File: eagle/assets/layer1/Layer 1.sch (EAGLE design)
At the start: 247 parts, among them M1C1 33nF, M1C2 680uF, M1C3 1.0uF, M1D1 RED, M1D2 BLUE, M1J1 XT30PB-F, M1Q1 AOD482, M1R1 1k, M1R10 1k, M1R11 10k, M1R12 4.7k, M1R2 1k, M1R3 3.3k, M1R4 3.3k, M1R5 1k, M1R6 1k, M1R7 1k, M1R8 10k, M1R9 10k, M2C1 33nF, M2C2 680uF, M2C3 1.0uF, M2D1 RED, M2D2 BLUE, M2J1 XT30PB-F, M2Q1 AOD482, M2R1 1k, M2R10 1k, M2R11 10k, M2R12 4.7k, M2R2 1k, M2R3 3.3k, M2R4 3.3k, M2R5 1k, M2R6 1k, M2R7 1k, M2R8 10k, M2R9 10k, M3C1 33nF, M3C2 680uF, M3C3 1.0uF, M3D1 RED, M3D2 BLUE, M3J1 XT30PB-F, M3Q1 AOD482, M3R1 1k, M3R10 1k, M3R11 10k, M3R12 4.7k, M3R2 1k, M3R3 3.3k, M3R4 3.3k, M3R5 1k, M3R6 1k, M3R7 1k, M3R8 10k, M3R9 10k, M4C1 33nF, M4C2 680uF, M4C3 1.0uF, M4D1 RED, M4D2 BLUE, M4J1 XT30PB-F, M4Q1 AOD482, M4R1 1k, M4R10 1k, M4R11 10k, M4R12 4.7k, M4R2 1k, M4R3 3.3k, M4R4 3.3k, M4R5 1k, M4R6 1k, M4R7 1k, M4R8 10k, M4R9 10k, Q1 LIGHT_SENSORALS, Q10 LIGHT_SENSORALS, Q11 LIGHT_SENSORALS, Q12 LIGHT_SENSORALS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

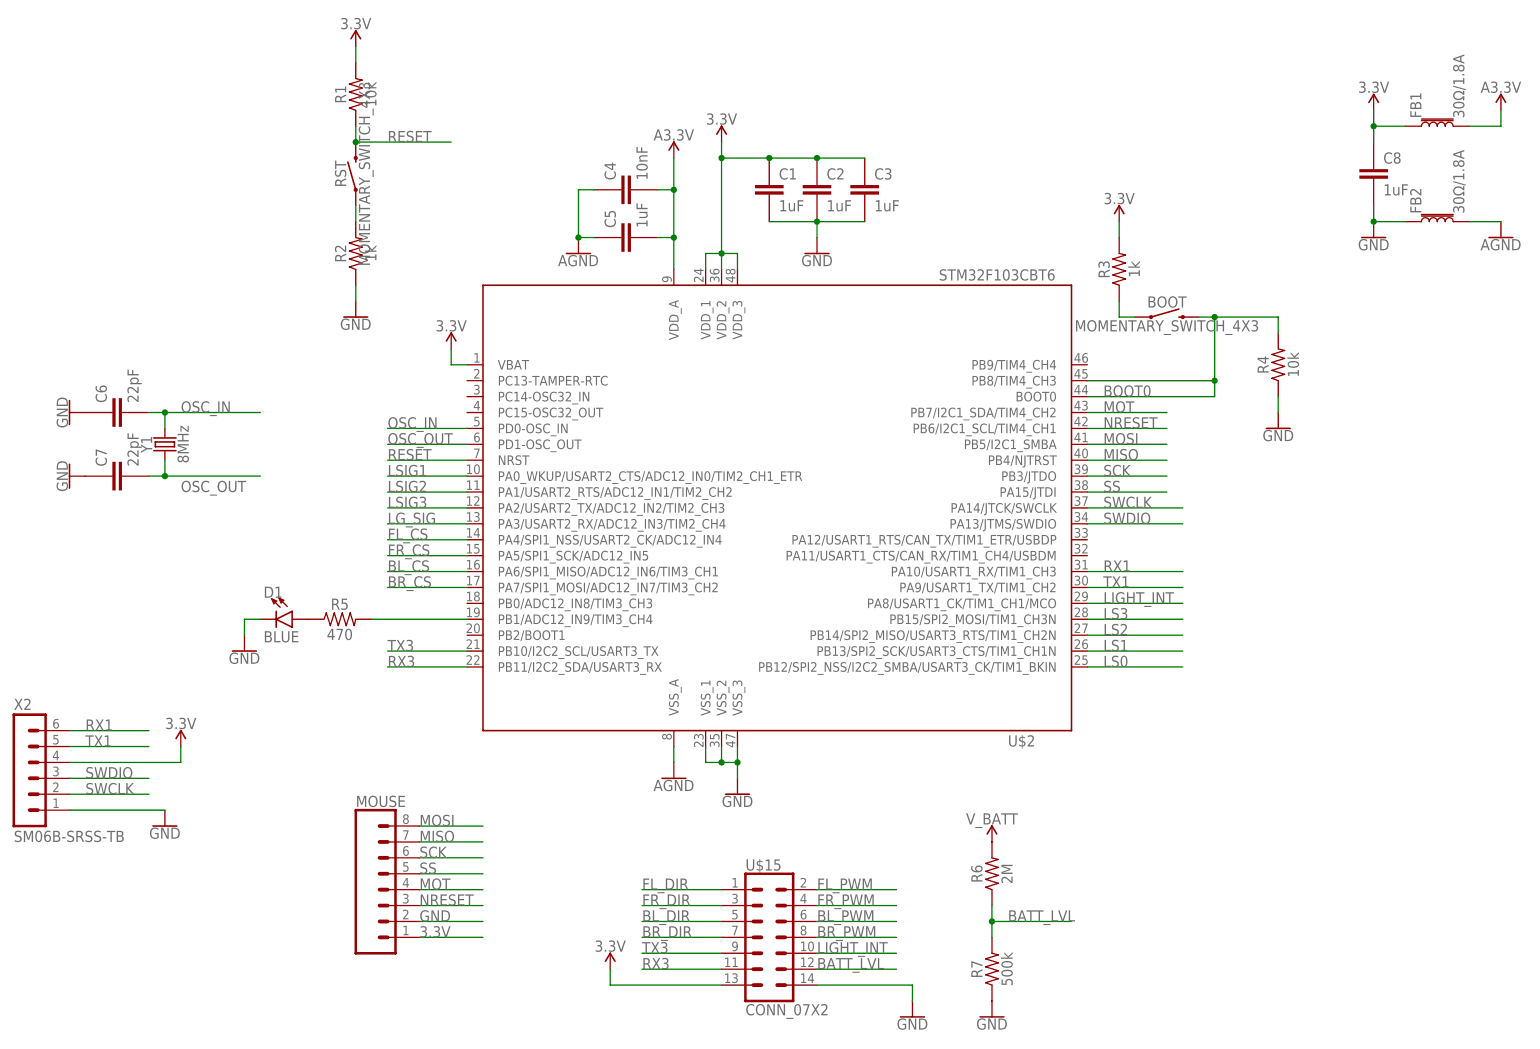
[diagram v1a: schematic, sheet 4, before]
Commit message: removed mouse sensor
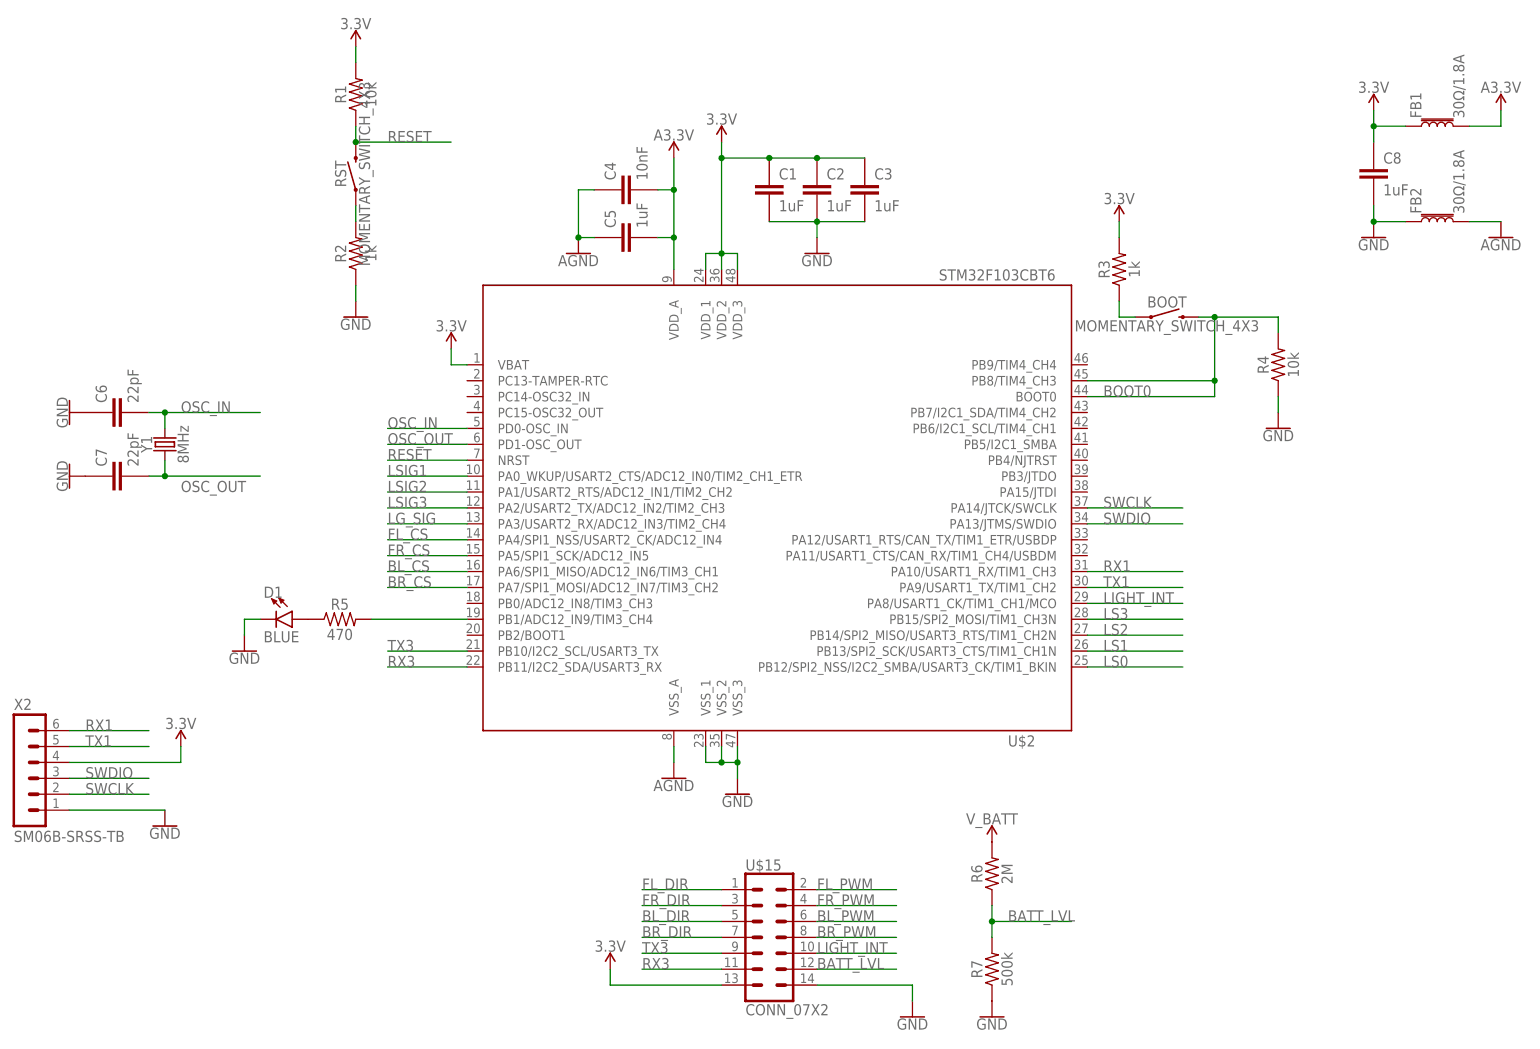
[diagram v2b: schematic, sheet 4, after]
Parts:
- removed LDR: (no value), SparkFun-Connectors:CONN_021X02_NO_SILK
- removed LED: (no value), SparkFun-Connectors:CONN_02POLAR
- removed LG_R2: 2k, JH:RESISTOR0603
- removed MOUSE: (no value), SparkFun-Connectors:CONN_08LOCK
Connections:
- removed net MISO: MOUSE.7, U$2.PB4/NJTRST
- removed net MOSI: MOUSE.8, U$2.PB5/I2C1_SMBA
- removed net MOT: MOUSE.4, U$2.PB7/I2C1_SDA/TIM4_CH2
- removed net NRESET: MOUSE.3, U$2.PB6/I2C1_SCL/TIM4_CH1
- removed net SCK: MOUSE.6, U$2.PB3/JTDO
- removed net SS: MOUSE.5, U$2.PA15/JTDI
- net 3.3V: no longer MOUSE.1
- net GND: no longer LED.1, LG_R2.1, MOUSE.2
- net LG_SIG: no longer LDR.2, LG_R2.2
- net LSWITCH: no longer LED.2
- net VCCA: no longer LDR.1

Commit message: depression
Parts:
- added LDR: (no value), SparkFun-Connectors:CONN_021X02_NO_SILK
- added LED: (no value), SparkFun-Connectors:CONN_02POLAR
- added LG_R2: 2k, JH:RESISTOR0603
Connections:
- net BL_OUTA: now also M3J1.V+; no longer M3J1.P$V+
- net BL_OUTB: now also M3J1.V-; no longer M3J1.P$V-
- net BR_OUTA: now also M4J1.V+; no longer M4J1.P$V+
- net BR_OUTB: now also M4J1.V-; no longer M4J1.P$V-
- net FL_OUTA: now also M1J1.V+; no longer M1J1.P$V+
- net FL_OUTB: now also M1J1.V-; no longer M1J1.P$V-
- net FR_OUTA: now also M2J1.V+; no longer M2J1.P$V+
- net FR_OUTB: now also M2J1.V-; no longer M2J1.P$V-
- net GND: now also ESC_OUT.V-, LED.1, LG_R2.1, U$1.V-; no longer ESC_OUT.P$V-, U$1.P$V-
- net LG_SIG: now also LDR.2, LG_R2.2
- net LSWITCH: now also LED.2
- net VCCA: now also LDR.1
- net V_BATT: now also ESC_OUT.V+, U$1.V+; no longer ESC_OUT.P$V+, U$1.P$V+

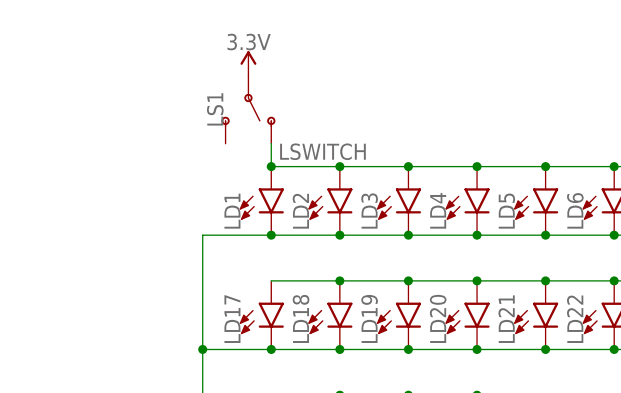
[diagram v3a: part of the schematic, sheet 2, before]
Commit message: edited layer 1
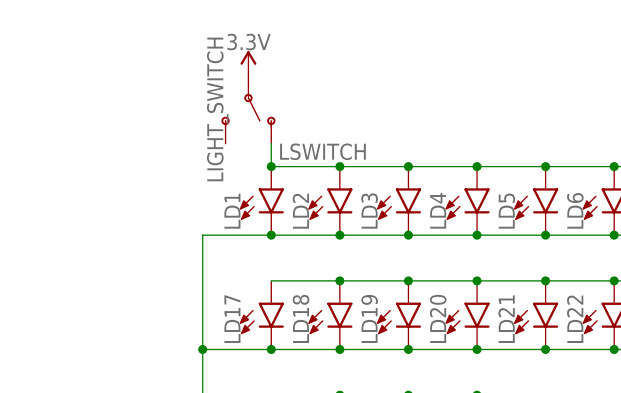
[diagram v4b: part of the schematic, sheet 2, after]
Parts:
- renumbered LS1 to LIGHT_SWITCH, S3 to MOTOR_SWITCH
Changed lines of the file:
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@@
 <part name="LD35" library="JH" library_urn="urn:adsk.eagle:library:6027132" deviceset="3528LED" device="" package3d_urn="urn:adsk.eagle:package:6740529/3"/>
 <part name="LD36" library="JH" library_urn="urn:adsk.eagle:library:6027132" deviceset="3528LED" device="" package3d_urn="urn:adsk.eagle:package:6740529/3"/>
-<part name="LS1" library="SparkFun-Switches" library_urn="urn:adsk.eagle:library:11044690" deviceset="SWITCH-SPDT" device="-PTH-11.6X4.0MM-LOCK" package3d_urn="urn:adsk.eagle:package:11044812/2"/>
+<part name="LIGHT_SWITCH" library="SparkFun-Switches" library_urn="urn:adsk.eagle:library:11044690" deviceset="SWITCH-SPDT" device="-PTH-11.6X4.0MM-LOCK" package3d_urn="urn:adsk.eagle:package:11044812/2"/>
 <part name="GND19" library="SparkFun-PowerSymbols" deviceset="GND" device=""/>
 <part name="LC1" library="JH" library_urn="urn:adsk.eagle:library:6027132" deviceset="CAPACITOR" device="0603" package3d_urn="urn:adsk.eagle:package:15441226/3" value="1uF"/>
@@
 <part name="SUPPLY15" library="SparkFun-PowerSymbols" deviceset="3.3V" device=""/>
 <part name="GND17" library="SparkFun-PowerSymbols" deviceset="GND" device=""/>
-<part name="S3" library="SparkFun-Switches" library_urn="urn:adsk.eagle:library:11044690" deviceset="SWITCH-SPDT" device="-PTH-11.6X4.0MM-LOCK" package3d_urn="urn:adsk.eagle:package:11044812/2"/>
+<part name="MOTOR_SWITCH" library="SparkFun-Switches" library_urn="urn:adsk.eagle:library:11044690" deviceset="SWITCH-SPDT" device="-PTH-11.6X4.0MM-LOCK" package3d_urn="urn:adsk.eagle:package:11044812/2"/>
 <part name="GND37" library="SparkFun-PowerSymbols" deviceset="GND" device=""/>
 <part name="M1J1" library="JH" library_urn="urn:adsk.eagle:library:6027132" deviceset="XT30" device="PB-F" package3d_urn="urn:adsk.eagle:package:15925142/7"/>
@@
 <attribute name="NAME" x="-120.269" y="135.128" size="1.778" layer="95" font="vector" rot="R90"/>
 </instance>
-<instance part="LS1" gate="1" x="-142.24" y="175.26" smashed="yes" rot="R270">
+<instance part="LIGHT_SWITCH" gate="1" x="-142.24" y="175.26" smashed="yes" rot="R270">
 <attribute name="NAME" x="-146.812" y="173.99" size="1.778" layer="95" font="vector" rot="R270" align="bottom-center"/>
 <attribute name="VALUE" x="-145.542" y="174.244" size="1.778" layer="96" font="vector" rot="R270" align="top-center"/>
@@
 <wire x1="-20.32" y1="142.24" x2="-20.32" y2="154.94" width="0.1524" layer="91"/>
 <junction x="-20.32" y="154.94"/>
-<pinref part="LS1" gate="1" pin="O"/>
+<pinref part="LIGHT_SWITCH" gate="1" pin="O"/>
 <wire x1="-139.7" y1="170.18" x2="-139.7" y2="167.64" width="0.1524" layer="91"/>
 <junction x="-139.7" y="167.64"/>
@@
 </segment>
 <segment>
-<pinref part="LS1" gate="1" pin="P"/>
+<pinref part="LIGHT_SWITCH" gate="1" pin="P"/>
 <pinref part="SUPPLY16" gate="G$1" pin="3.3V"/>
 </segment>
@@
 <attribute name="VALUE" x="50.8" y="53.086" size="1.778" layer="96" align="top-center"/>
 </instance>
-<instance part="S3" gate="1" x="22.86" y="55.88" smashed="yes" rot="R270">
+<instance part="MOTOR_SWITCH" gate="1" x="22.86" y="55.88" smashed="yes" rot="R270">
 <attribute name="NAME" x="25.908" y="54.61" size="1.778" layer="95" font="vector" rot="R270" align="bottom-center"/>
 <attribute name="VALUE" x="19.558" y="54.864" size="1.778" layer="96" font="vector" rot="R270" align="top-center"/>
@@
 </segment>
 <segment>
-<pinref part="S3" gate="1" pin="P"/>
+<pinref part="MOTOR_SWITCH" gate="1" pin="P"/>
 <wire x1="22.86" y1="58.42" x2="22.86" y2="66.04" width="0.1524" layer="91"/>
 <label x="22.86" y="60.96" size="1.778" layer="95"/>
@@
 </segment>
 <segment>
-<pinref part="S3" gate="1" pin="O"/>
+<pinref part="MOTOR_SWITCH" gate="1" pin="O"/>
 <pinref part="GND37" gate="1" pin="GND"/>
 </segment>

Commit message: redid layer 1
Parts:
- D1: value BLUE -> STM_LED
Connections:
- net N$73: now also U$2.PB0/ADC12_IN8/TIM3_CH3; no longer U$2.PB1/ADC12_IN9/TIM3_CH4
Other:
- moved on the sheet: D1, R5
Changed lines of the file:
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@@
 <part name="GND31" library="SparkFun-PowerSymbols" deviceset="GND" device=""/>
 <part name="R5" library="JH" library_urn="urn:adsk.eagle:library:6027132" deviceset="RESISTOR" device="0603" package3d_urn="urn:adsk.eagle:package:15441228/3" value="470"/>
-<part name="D1" library="SparkFun-LED" library_urn="urn:adsk.eagle:library:11010284" deviceset="LED" device="0603" package3d_urn="urn:adsk.eagle:package:11010371/2" value="BLUE"/>
+<part name="D1" library="SparkFun-LED" library_urn="urn:adsk.eagle:library:11010284" deviceset="LED" device="0603" package3d_urn="urn:adsk.eagle:package:11010371/2" value="STM_LED"/>
 <part name="GND32" library="SparkFun-PowerSymbols" deviceset="GND" device=""/>
 <part name="SUPPLY19" library="SparkFun-PowerSymbols" deviceset="3.3V" device=""/>
@@
 <attribute name="VALUE" x="-27.94" y="103.886" size="1.778" layer="96" align="top-center"/>
 </instance>
-<instance part="R5" gate="G$1" x="-177.8" y="73.66" smashed="yes">
-<attribute name="NAME" x="-177.8" y="75.184" size="1.778" layer="95" font="vector" align="bottom-center"/>
-<attribute name="VALUE" x="-177.8" y="72.136" size="1.778" layer="96" font="vector" align="top-center"/>
-</instance>
-<instance part="D1" gate="D1" x="-185.42" y="73.66" smashed="yes" rot="R270">
-<attribute name="NAME" x="-189.992" y="77.089" size="1.778" layer="95" font="vector"/>
-<attribute name="VALUE" x="-189.992" y="71.755" size="1.778" layer="96" font="vector" align="top-left"/>
+<instance part="R5" gate="G$1" x="-175.26" y="76.2" smashed="yes">
+<attribute name="NAME" x="-175.26" y="77.724" size="1.778" layer="95" font="vector" align="bottom-center"/>
+<attribute name="VALUE" x="-175.26" y="74.676" size="1.778" layer="96" font="vector" align="top-center"/>
+</instance>
+<instance part="D1" gate="D1" x="-182.88" y="76.2" smashed="yes" rot="R270">
+<attribute name="NAME" x="-187.452" y="79.629" size="1.778" layer="95" font="vector"/>
+<attribute name="VALUE" x="-187.452" y="74.295" size="1.778" layer="96" font="vector" align="top-left"/>
 </instance>
-<instance part="GND32" gate="1" x="-193.04" y="68.58" smashed="yes">
-<attribute name="VALUE" x="-193.04" y="68.326" size="1.778" layer="96" align="top-center"/>
+<instance part="GND32" gate="1" x="-190.5" y="71.12" smashed="yes">
+<attribute name="VALUE" x="-190.5" y="70.866" size="1.778" layer="96" align="top-center"/>
 </instance>
 <instance part="SUPPLY19" gate="G$1" x="-53.34" y="137.16" smashed="yes">
@@
 <segment>
 <pinref part="D1" gate="D1" pin="C"/>
-<wire x1="-190.5" y1="73.66" x2="-193.04" y2="73.66" width="0.1524" layer="91"/>
+<wire x1="-187.96" y1="76.2" x2="-190.5" y2="76.2" width="0.1524" layer="91"/>
 <pinref part="GND32" gate="1" pin="GND"/>
-<wire x1="-193.04" y1="73.66" x2="-193.04" y2="71.12" width="0.1524" layer="91"/>
+<wire x1="-190.5" y1="76.2" x2="-190.5" y2="73.66" width="0.1524" layer="91"/>
 </segment>
 <segment>
@@
 </segment>
 </net>
-<net name="N$73" class="0">
-<segment>
-<pinref part="U$2" gate="G$1" pin="PB1/ADC12_IN9/TIM3_CH4"/>
-<wire x1="-157.48" y1="73.66" x2="-172.72" y2="73.66" width="0.1524" layer="91"/>
-<pinref part="R5" gate="G$1" pin="2"/>
-</segment>
-</net>
 <net name="N$74" class="0">
 <segment>
@@
 </segment>
 </net>
+<net name="N$73" class="0">
+<segment>
+<pinref part="U$2" gate="G$1" pin="PB0/ADC12_IN8/TIM3_CH3"/>
+<wire x1="-157.48" y1="76.2" x2="-170.18" y2="76.2" width="0.1524" layer="91"/>
+<pinref part="R5" gate="G$1" pin="2"/>
+</segment>
+</net>

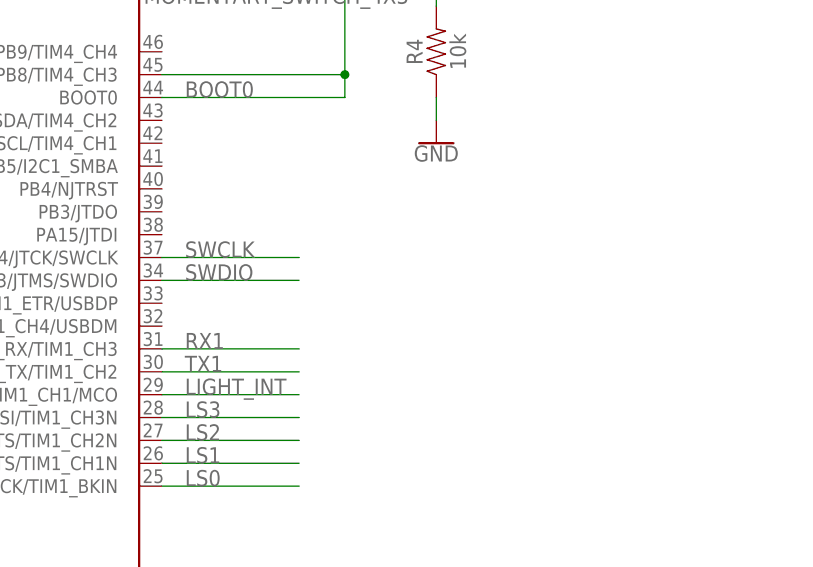
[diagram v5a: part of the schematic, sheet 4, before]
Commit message: Added limit switch
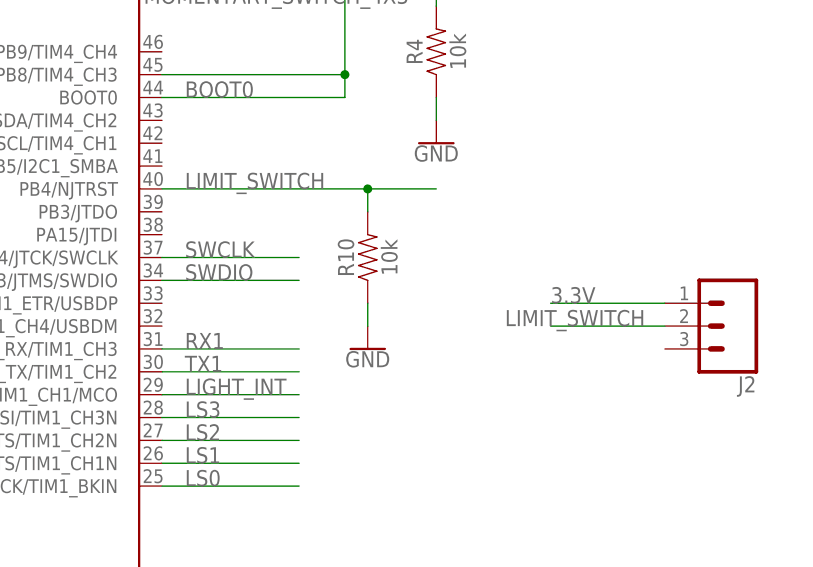
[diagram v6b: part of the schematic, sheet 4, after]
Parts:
- added J2: (no value), SparkFun-Connectors:CONN_03LOCK_NO_SILK
- added R10: 10k, JH:RESISTOR0603
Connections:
- new net LIMIT_SWITCH: J2.2, R10.2, U$2.PB4/NJTRST
- net 3.3V: now also J2.1
- net GND: now also R10.1
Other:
- note added: "LIMIT_SWITCH"
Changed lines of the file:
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@@
 <part name="LED" library="SparkFun-Connectors" library_urn="urn:adsk.eagle:library:11010760" deviceset="CONN_02" device="POLAR" package3d_urn="urn:adsk.eagle:package:11011251/1"/>
 <part name="U$7" library="SparkFun-PowerSymbols" deviceset="VCCA" device="" value="A3.3V"/>
+<part name="J2" library="SparkFun-Connectors" library_urn="urn:adsk.eagle:library:513" deviceset="CONN_03" device="LOCK_NO_SILK" package3d_urn="urn:adsk.eagle:package:38074/1"/>
+<part name="R10" library="JH" library_urn="urn:adsk.eagle:library:6027132" deviceset="RESISTOR" device="0603" package3d_urn="urn:adsk.eagle:package:15441228/3" value="10k"/>
+<part name="GND40" library="SparkFun-PowerSymbols" deviceset="GND" device=""/>
 </parts>
 <sheets>
@@
 <sheet>
 <plain>
+<text x="-55.88" y="99.06" size="1.778" layer="95">LIMIT_SWITCH</text>
 </plain>
 <instances>
@@
 <attribute name="VALUE" x="-72.136" y="17.78" size="1.778" layer="96" font="vector" rot="R90" align="top-center"/>
 </instance>
+<instance part="J2" gate="J$1" x="5.08" y="83.82" smashed="yes" rot="R180">
+<attribute name="VALUE" x="7.62" y="91.186" size="1.778" layer="96" font="vector" rot="R180"/>
+<attribute name="NAME" x="7.62" y="78.232" size="1.778" layer="95" font="vector" rot="R180"/>
+</instance>
+<instance part="R10" gate="G$1" x="-35.56" y="91.44" smashed="yes" rot="R90">
+<attribute name="NAME" x="-37.084" y="91.44" size="1.778" layer="95" font="vector" rot="R90" align="bottom-center"/>
+<attribute name="VALUE" x="-34.036" y="91.44" size="1.778" layer="96" font="vector" rot="R90" align="top-center"/>
+</instance>
+<instance part="GND40" gate="1" x="-35.56" y="81.28" smashed="yes">
+<attribute name="VALUE" x="-35.56" y="81.026" size="1.778" layer="96" align="top-center"/>
+</instance>
 </instances>
 <busses>
@@
 <pinref part="X2" gate="G$1" pin="4"/>
 </segment>
+<segment>
+<pinref part="J2" gate="J$1" pin="1"/>
+<wire x1="-2.54" y1="86.36" x2="-15.24" y2="86.36" width="0.1524" layer="91"/>
+<label x="-15.24" y="86.36" size="1.778" layer="95"/>
+</segment>
 </net>
 <net name="GND" class="0">
@@
 <pinref part="R7" gate="G$1" pin="1"/>
 </segment>
+<segment>
+<pinref part="R10" gate="G$1" pin="1"/>
+<pinref part="GND40" gate="1" pin="GND"/>
+<wire x1="-35.56" y1="86.36" x2="-35.56" y2="83.82" width="0.1524" layer="91"/>
+</segment>
 </net>
 <net name="SWDIO" class="0">
@@
 </segment>
 </net>
+<net name="LIMIT_SWITCH" class="0">
+<segment>
+<pinref part="J2" gate="J$1" pin="2"/>
+<wire x1="-15.24" y1="83.82" x2="-2.54" y2="83.82" width="0.1524" layer="91"/>
+<label x="-20.32" y="83.82" size="1.778" layer="95"/>
+</segment>
+<segment>
+<pinref part="R10" gate="G$1" pin="2"/>
+<wire x1="-35.56" y1="99.06" x2="-27.94" y2="99.06" width="0.1524" layer="91"/>
+<wire x1="-35.56" y1="96.52" x2="-35.56" y2="99.06" width="0.1524" layer="91"/>
+<pinref part="U$2" gate="G$1" pin="PB4/NJTRST"/>
+<wire x1="-58.42" y1="99.06" x2="-35.56" y2="99.06" width="0.1524" layer="91"/>
+<junction x="-35.56" y="99.06"/>
+</segment>
+</net>
